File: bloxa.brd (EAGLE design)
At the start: 24.9 x 33.6 mm, 89 parts, among them CON1 PINHEAD_1X02-2.54, CON7 CON-4P-JST_GH-RA, CON8 CON-4P-JST_GH-RA, IC1 TPD3S014DBVR-SOT23-6, IC2 TJA1051(X)/3-SO8, IC6 MCP9700, Q13 BUK9K6R2-40E,115, Q14 BUK9K6R2-40E,115, Q15 BUK9K6R2-40E,115

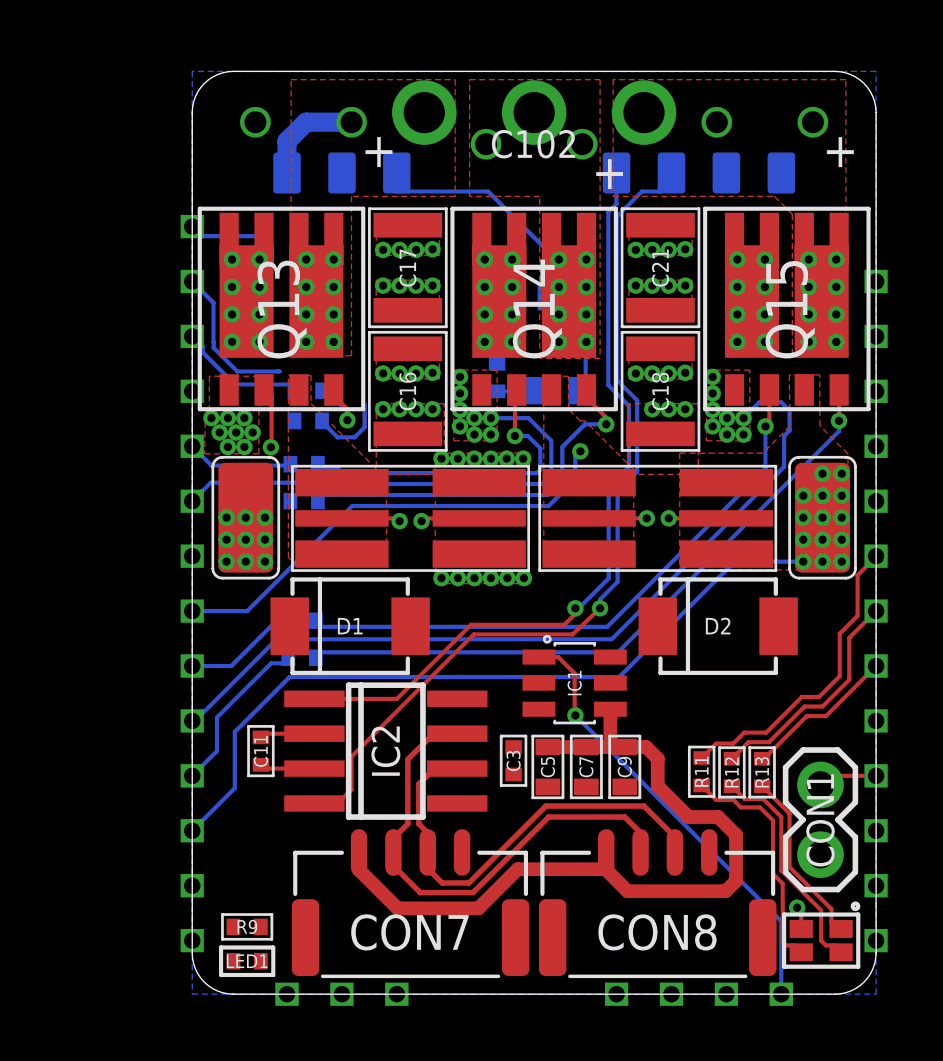
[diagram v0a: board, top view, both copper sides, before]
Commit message: all components moved to top side
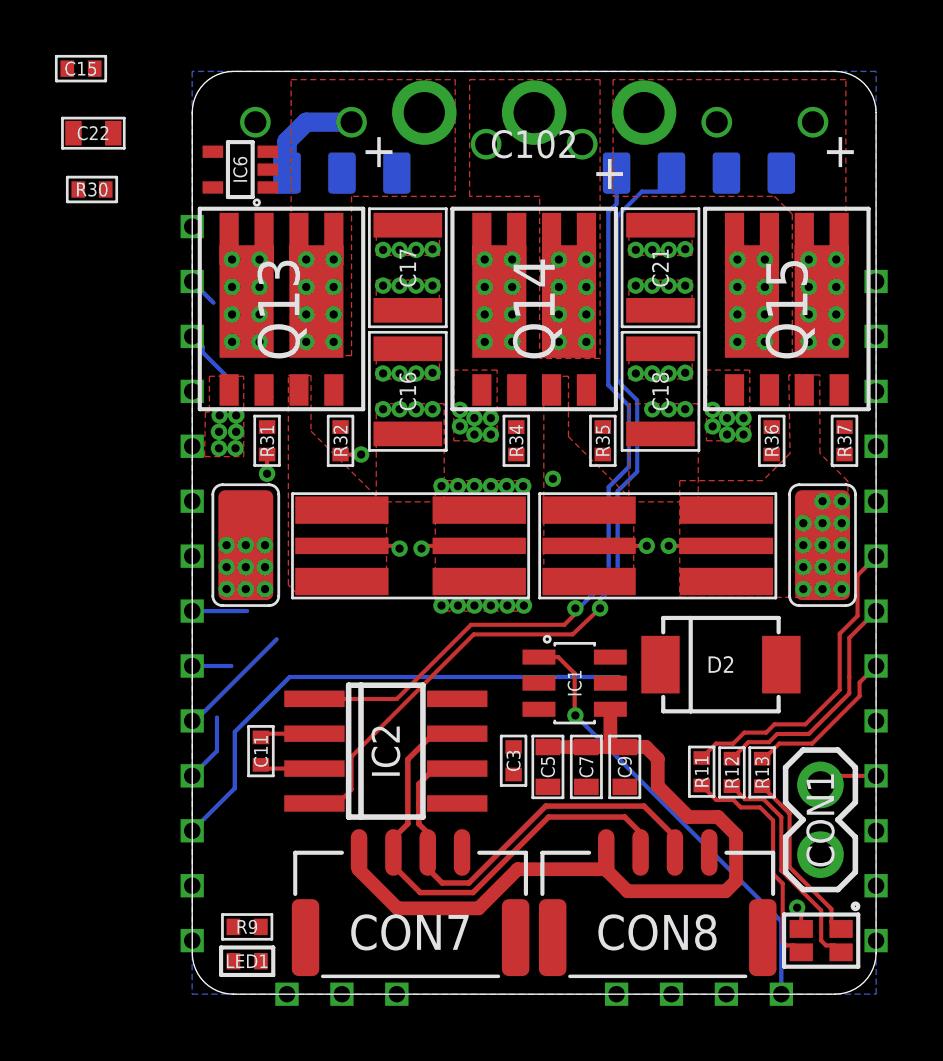
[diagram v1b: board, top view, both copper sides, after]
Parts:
- removed D1: PTVS36VP1UP,115-36V-SOD128, TVS_diodes:SOD128
- IC6: value MCP9700 -> MCP9700-SC70-5; device myxa_masterlib:SOT23B-3 -> misc:SC70-5
- moved R37 21.3 mm to (11.3, 5.20), flipped to the top, turned to 90 degrees
- moved C15 18.9 mm to (-16.5, 18.8), flipped to the top, turned to 180 degrees
- moved R36 18.3 mm to (8.65, 5.20), flipped to the top, turned to 90 degrees
- moved C22 18.2 mm to (-16.1, 16.4), flipped to the top
- moved R30 17.7 mm to (-16.1, 14.3), flipped to the top
- moved IC6 13.4 mm to (-10.7, 15.1), flipped to the top, turned to 180 degrees
- moved R35 11.1 mm to (2.50, 5.20), flipped to the top, turned to 90 degrees
- moved R34 7.77 mm to (-0.65, 5.20), flipped to the top, turned to 90 degrees
- moved R32 2.17 mm to (-7.05, 5.20), flipped to the top, turned to 90 degrees
- moved R31 1.67 mm to (-9.72, 5.20), flipped to the top, turned to 90 degrees
- moved D2 1.40 mm to (6.80, -2.95)
- moved BAT+ 1.00 mm to (-10.5, 1.40)
- moved BAT- 1.00 mm to (10.5, 1.40)
- moved R26 1.00 mm to (-4.50, 1.38)
- moved R33 1.00 mm to (4.50, 1.38)
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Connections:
- net N$1: now also IC6.4; no longer IC6.1
- net PGND: now also IC6.2; no longer D1.A, IC6.3
- net TEMPERATURE_SENSOR: now also IC6.3; no longer IC6.2
- net VDC: no longer D1.C
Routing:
- net PHASE_C: track 29.6 -> 4.31 mm, vias 16 -> 14
- net N$29: track 24.0 -> 0.00 mm, vias 1 -> 0
- net N$28: track 21.8 -> 0.00 mm, vias 1 -> 0
- net PHASE_B: track 18.4 -> 1.12 mm, vias 16 -> 14
- net PHASE_B_GND: track 17.0 -> 2.00 mm
- net N$31: track 14.1 -> 0.28 mm, vias 1 -> 0
- net N$30: track 11.9 -> 0.09 mm, vias 1 -> 0
- net PHASE_C_GND: track 27.5 -> 19.1 mm
- net VDD_5V: track 10.5 -> 2.84 mm
- net PHASE_A_GATE_HIGH: track 5.56 -> 0.70 mm, vias 0 -> 1
- net N$1: track 4.69 -> 0.00 mm
- net PHASE_A: track 5.96 -> 1.55 mm, vias 16 -> 14
- net PHASE_B_GATE_HIGH: track 3.89 -> 0.00 mm
- net PHASE_C_GATE_LOW: track 6.06 -> 2.50 mm
- net PHASE_C_GATE_HIGH: track 4.18 -> 1.42 mm
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
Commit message: routing complete
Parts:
- removed C22: 4.7µF, C_digikey:C0603
- removed R30: 200R, R_digikey:R0402
- added C1: 0.1µF, C_digikey:C0402
- moved C15 6.25 mm to (-10.3, 18.0), turned to 0 degrees
- moved R13 3.65 mm to (11.2, -4.70)
- moved S2 3.20 mm to (9.80, 3.00), flipped to the bottom
- moved R11 1.31 mm to (7.40, -6.97)
- moved R12 1.28 mm to (8.47, -6.97)
- moved C9 1.16 mm to (4.45, -6.55)
- moved C5 1.16 mm to (1.65, -6.55)
- moved C7 1.16 mm to (3.05, -6.55)
- moved C11 1.05 mm to (-9.95, -5.05)
- moved IC2 1.00 mm to (-5.40, -5.10)
- moved C3 0.72 mm to (-0.33, -5.88), turned to 180 degrees
- moved R34 0.30 mm to (-0.35, 5.20)
- moved R9 0.25 mm to (-10.4, -12.2), turned to 180 degrees
- moved D2 0.18 mm to (6.95, -2.85)
- turned LED1 to 0 degrees
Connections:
- removed net N$1: C22.P$2, IC6.4, R30.1
- removed net N$5: CON7.4, CON8.4
- net GND: no longer C11.2, C3.2, IC2.2
- net GNDD: now also CON7.4, CON8.4
- net PGND: now also C1.2, C11.2, C15.2, C3.2, IC2.2; no longer C15.1, C22.P$1
- net TEMPERATURE_SENSOR: now also C1.1; no longer C15.2
- net VDD_5V: now also C15.1, IC6.4; no longer R30.2
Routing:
- net VDD_5V: track 2.84 -> 76.3 mm, vias 1 -> 8
- net CAN1_LED: track 0.00 -> 45.8 mm, vias 0 -> 1
- net TEMPERATURE_SENSOR: track 0.00 -> 41.0 mm, vias 0 -> 2
- net PHASE_C_GATE_LOW: track 2.50 -> 29.7 mm, vias 0 -> 1
- net PHASE_C_GATE_HIGH: track 1.42 -> 25.0 mm, vias 0 -> 1
- net PHASE_C: track 4.31 -> 27.0 mm
- net PHASE_B_GATE_LOW: track 0.00 -> 20.5 mm, vias 0 -> 1
- net PHASE_B_GATE_HIGH: track 0.00 -> 14.7 mm, vias 0 -> 1
- net PHASE_B_GND: track 2.00 -> 16.4 mm
- net PGND: track 0.00 -> 13.0 mm, vias 40 -> 44
- net PHASE_B: track 1.12 -> 13.3 mm
- net PHASE_A_GATE_HIGH: track 0.70 -> 11.8 mm
- net PHASE_C_GND: track 19.1 -> 28.7 mm
- net PHASE_A_GATE_LOW: track 3.14 -> 12.8 mm
- net PHASE_A_GND: track 0.00 -> 9.05 mm, vias 0 -> 1
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- added copper zone on layer 1, net GNDD
- added copper zone on layer 16, net GNDD
- added copper zone on layer 15, net PHASE_A
- added copper zone on layer 15, net PHASE_B
- added copper zone on layer 15, net PHASE_C

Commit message: UPDATES
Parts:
- added U$1: CONNECTION, misc:CONNECTION
- added U$8, U$9: FIDUCIALMOUNT, usb2can_master_lib:FIDUCIA-MOUNT
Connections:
- net GNDD: now also U$1.P$2
- net PGND: now also U$1.P$1
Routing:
- net TEMPERATURE_SENSOR: track 41.0 -> 42.2 mm
- net VDD_5V: track 76.3 -> 75.4 mm
- net VDC: vias 52 -> 50
- net PGND: vias 44 -> 49
- net GNDD: vias 9 -> 12
- added copper zone on layer 1, net VDD_5V
- added copper zone on layer 15, net VDD_5V
- added copper zone on layer 16, net VDD_5V

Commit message: More polygones updates
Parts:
- added U$3: CONNECTION, misc:CONNECTION
- moved U$1 3.99 mm to (-6.78, -7.80), turned to 180 degrees
- turned CON1 to 270 degrees
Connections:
- net GND: now also C1.2, C11.2, C3.2, CON1.1, IC2.2, U$1.P$1, U$3.P$1
- net PGND: now also U$3.P$2; no longer C1.2, C11.2, C3.2, CON1.1, IC2.2, U$1.P$1
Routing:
- net PGND: track 13.0 -> 4.58 mm, vias 49 -> 38
- net GND: track 0.00 -> 6.58 mm, vias 0 -> 8
- net PHASE_B_CURRENT_SHUNT_P: track 24.1 -> 29.3 mm
- net PHASE_B_CURRENT_SHUNT_N: track 24.1 -> 29.0 mm
- net GNDD: track 0.05 -> 2.55 mm, vias 12 -> 10
- net PHASE_C_GATE_LOW: track 29.7 -> 32.0 mm
- net PHASE_C_GND: track 28.7 -> 30.7 mm
- net GPIO1: track 2.16 -> 3.71 mm
- net PHASE_C: track 27.0 -> 28.4 mm
- net VDD_5V: track 75.4 -> 76.4 mm
- net PHASE_A_GND: track 9.20 -> 9.96 mm
- net TEMPERATURE_SENSOR: track 42.2 -> 42.9 mm
- net CAN1_RX: track 30.6 -> 31.3 mm
- net VDC: vias 50 -> 49
- added copper zone on layer 15, net GND
- added copper zone on layer 16, net GND
- added copper zone on layer 15, net GNDD
- added copper zone on layer 16, net PHASE_A
- added copper zone on layer 16, net PHASE_B
- added copper zone on layer 16, net PHASE_C
- added copper zone on layer 15, net VDC
- added copper zone on layer 16, net VDC
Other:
- board text added: "BLOXA 0.1"

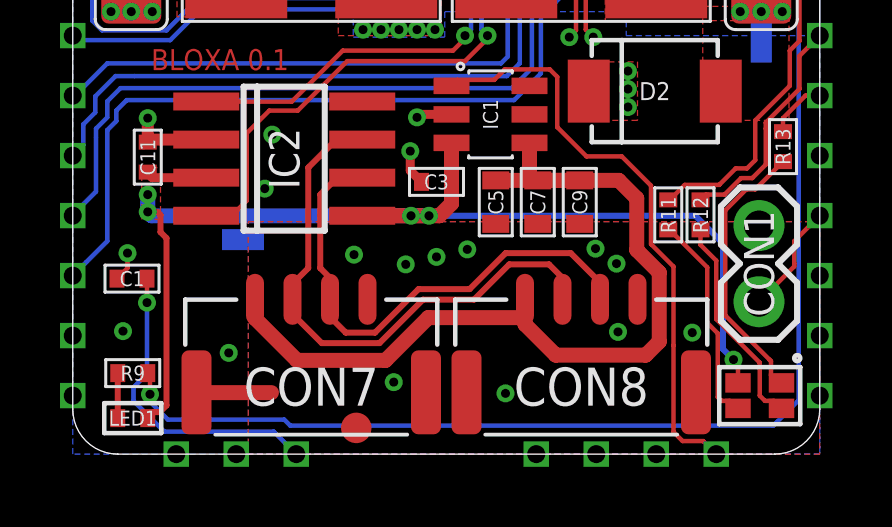
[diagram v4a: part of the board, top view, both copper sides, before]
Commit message: alternate footprints for LED fancy placement
Will never use it probably
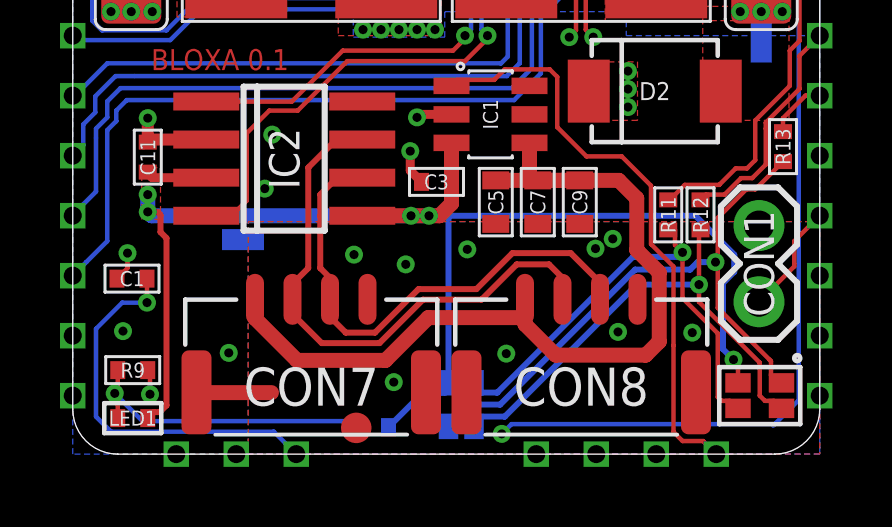
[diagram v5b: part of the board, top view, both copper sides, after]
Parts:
- added LED2: GREEN, myxa_masterlib:0402_LED
- added LED4: LTST-C19HE1WT, myxa_masterlib:LITE_ON_RGB_LED
- moved R9 0.10 mm to (-10.4, -12.2)
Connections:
- removed net N$59: LED3.G, R12.1
- new net N$4: LED3.G, LED4.G, R12.1
- net N$17: now also LED2.C
- net N$58: now also LED4.R
- net N$60: now also LED4.B
- net VDD_5V: now also LED2.A, LED4.+
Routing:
- net N$4: track 0.00 -> 16.9 mm, vias 0 -> 1
- net N$58: track 9.18 -> 20.8 mm, vias 0 -> 1
- net N$60: track 7.12 -> 16.5 mm, vias 0 -> 1
- net N$17: track 1.50 -> 10.3 mm, vias 0 -> 1
- net VDD_5V: track 76.4 -> 85.0 mm
- net N$59: track 7.24 -> 0.00 mm
- net TEMPERATURE_SENSOR: track 42.9 -> 45.5 mm
- net CAN1_LED: track 45.8 -> 46.1 mm, vias 1 -> 2
- net GNDD: vias 10 -> 9

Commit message: Renaming
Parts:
- removed C100, C101: 180µF, rc:RADIAL_SIDE_8X21.5
- removed C15: 0.1µF, C_digikey:C0402
- removed C16, C18: 10µF, C_digikey:C1210
- removed CON7: CON-4P-JST_GH-RA, Connectors:JST_GH-4P-RA
- removed IC6: MCP9700-SC70-5, misc:SC70-5
- removed R35, R36, R37: 4R3, R_digikey:R0402
- removed U$8, U$9: FIDUCIALMOUNT, usb2can_master_lib:FIDUCIA-MOUNT
- added C10, C4: 0.1µF, C_digikey:C0402
- added C12, C13, C14: 4.7µF, C_digikey:C0603
- added CON3: PINHEAD_1X02-2.54, pinhead:1X02-PTH-2.54
- added FD1, FD2: FIDUCIALMOUNT, misc:FIDUCIA-MOUNT
- added IC3: TJA1051(X)/3-SO8, serial_interfaces:SOIC8
- added R3, R5, R6: 1K, R_digikey:R0402
- C1, C3: value 0.1µF -> 180µF; device C_digikey:C0402 -> rc:RADIAL_SIDE_8X21.5
- C5: value 4.7µF -> 0.1µF; device C_digikey:C0603 -> C_digikey:C0402
- C7, C9: value 4.7µF -> 10µF; device C_digikey:C0603 -> C_digikey:C1210
- CON1: value PINHEAD_1X02-2.54 -> CON-4P-JST_GH-RA; device pinhead:1X02-PTH-2.54 -> Connectors:JST_GH-4P-RA
- IC1: value TPD3S014DBVR-SOT23-6 -> MCP9700-SC70-5; device myxa_masterlib:SOT26 -> misc:SC70-5
- IC2: value TJA1051(X)/3-SO8 -> TPD3S014DBVR-SOT23-6; device serial_interfaces:SOIC8 -> myxa_masterlib:SOT26
- PAD22, PAD23, PAD24, PAD4: value PAD-HOLE-0.6 -> PAD-1X1.5; device PADS:HOLE_0.6 -> PADS:SMD_1X1,5
- PAD38, PAD39, PAD40, PAD41: value PAD-1X1.5 -> PAD-HOLE-0.6; device PADS:SMD_1X1,5 -> PADS:HOLE_0.6
- R11, R12, R9: value 1K -> 4R3
- moved PAD25 36.0 mm to (-12.4, 13.0)
- moved PAD38 35.2 mm to (-12.4, -13.0)
- moved PAD24 34.9 mm to (-9.00, 14.9)
- moved PAD39 33.9 mm to (-9.00, -14.9)
- moved PAD26 33.2 mm to (-12.4, 11.0)
- moved PAD37 33.2 mm to (-12.4, -11.0)
- moved PAD23 33.0 mm to (-7.00, 14.9)
- moved PAD40 32.2 mm to (-7.00, -14.9)
- moved PAD22 31.5 mm to (-5.00, 14.9)
- moved PAD41 31.0 mm to (-5.00, -14.9)
- moved PAD27 30.7 mm to (-12.4, 9.00)
- moved PAD36 30.7 mm to (-12.4, -9.00)
- moved PAD28 28.6 mm to (-12.4, 7.00)
- moved PAD35 28.6 mm to (-12.4, -7.00)
- moved C5 27.3 mm to (-10.3, 18.0), turned to 0 degrees
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- renumbered A to PAD44, B to PAD45, BAT+ to PAD42, BAT- to PAD43, C to PAD46, C102 to C2, C17 to C8, C21 to C6, CON8 to CON2, D2 to D1, Q13 to Q1, Q14 to Q2, Q15 to Q3, R13 to R7, R26 to R4, R31 to R1, R32 to R2, R33 to R10, R34 to R8, S2 to S1, U$1 to J2, U$3 to J1
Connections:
- net BEC_ENABLE_OUT: now also IC2.1, PAD21.P$1; no longer IC1.1, PAD24.P$1
- net CAN1_LED: now also PAD6.P$1, R3.1; no longer PAD36.P$1, R9.1
- net CAN1_RX: now also IC3.4, PAD2.P$1; no longer IC2.4, PAD40.P$1
- net CAN1_TX: now also IC3.1, PAD1.P$1; no longer IC2.1, PAD41.P$1
- net CAN1_VDD: now also C12.P$2, C13.P$2, C14.P$2, CON1.1, IC2.4; no longer C5.P$2, C7.P$2, C9.P$2, CON7.1, IC1.4
- net CAN2_LED: now also PAD5.P$1; no longer PAD37.P$1
- net CAN2_RX: now also PAD4.P$1; no longer PAD38.P$1
- net CAN2_TX: now also PAD3.P$1; no longer PAD39.P$1
- net EN_GATE_OUT: now also PAD16.P$1; no longer PAD26.P$1
- net GAIN_OUT: now also PAD17.P$1; no longer PAD25.P$1
- net GND: now also C10.2, C4.2, CON3.1, IC3.2; no longer C1.2, C3.2, CON1.1, IC1.2
- net GNDD: now also C12.P$1, C13.P$1, C14.P$1, CON1.4, CON1.M$0, CON1.M$1; no longer C5.P$1, C7.P$1, C9.P$1, CON7.4, CON7.M$0, CON7.M$1
- net GPIO1: now also CON3.2, PAD14.P$1; no longer CON1.2, PAD28.P$1
- net GPIO2: now also PAD15.P$1; no longer PAD27.P$1
- net N$17: now also R3.2; no longer R9.2
- net N$2: now also IC3.8; no longer IC2.8
- net N$22: now also CON1.2, IC3.7; no longer CON7.2, IC2.7
- net N$23: now also CON1.3, IC3.6; no longer CON7.3, IC2.6
- net N$28: now also R11.2; no longer R36.2
- net N$29: now also R12.2; no longer R37.2
- net N$31: now also R9.2; no longer R35.2
- net N$4: now also R6.1; no longer R12.1
- net N$60: now also R5.1; no longer R11.1
- net OVERCURRENT_PROTECT_ADJ: now also PAD13.P$1; no longer PAD29.P$1
- net PGND: now also C1.-, C3.-, C5.2, C7.1, C9.1, IC1.2, PAD23.P$1; no longer C100.-, C101.-, C15.2, C16.1, C18.1, IC6.2, PAD2.P$1
- net PHASE_A: now also PAD26.P$1; no longer PAD5.P$1
- net PHASE_A_CURRENT_SHUNT_N: now also PAD37.P$1; no longer PAD16.P$1
- net PHASE_A_CURRENT_SHUNT_P: now also PAD38.P$1; no longer PAD17.P$1
- net PHASE_A_GATE_HIGH: now also PAD25.P$1; no longer PAD4.P$1
- net PHASE_A_GATE_LOW: now also PAD27.P$1; no longer PAD6.P$1
- net PHASE_A_GND: now also PAD28.P$1; no longer PAD7.P$1
- net PHASE_B: now also PAD30.P$1; no longer PAD9.P$1
- net PHASE_B_CURRENT_SHUNT_N: now also PAD39.P$1; no longer PAD18.P$1
- net PHASE_B_CURRENT_SHUNT_P: now also PAD40.P$1; no longer PAD19.P$1
- net PHASE_B_GATE_HIGH: now also PAD29.P$1; no longer PAD8.P$1
- net PHASE_B_GATE_LOW: now also PAD31.P$1, R9.1; no longer PAD10.P$1, R35.1
- net PHASE_B_GND: now also PAD32.P$1; no longer PAD11.P$1
- net PHASE_C: now also PAD34.P$1; no longer PAD13.P$1
- net PHASE_C_GATE_HIGH: now also PAD33.P$1, R11.1; no longer PAD12.P$1, R36.1
- net PHASE_C_GATE_LOW: now also PAD35.P$1, R12.1; no longer PAD14.P$1, R37.1
- net PHASE_C_GND: now also PAD36.P$1; no longer PAD15.P$1
- net POWER_ENABLE_IN: now also PAD18.P$1; no longer PAD21.P$1
- net RGB_LED_B: now also PAD10.P$1, R5.2; no longer PAD32.P$1, R11.2
- net RGB_LED_G: now also PAD11.P$1, R6.2; no longer PAD31.P$1, R12.2
- net RGB_LED_R: now also PAD12.P$1; no longer PAD30.P$1
- net TEMPERATURE_SENSOR: now also C4.1, IC1.3, PAD41.P$1; no longer C1.1, IC6.3, PAD20.P$1
- net USART_RX: now also PAD20.P$1; no longer PAD23.P$1
- net USART_TX: now also PAD19.P$1; no longer PAD22.P$1
- net USB+: now also PAD7.P$1; no longer PAD35.P$1
- net USB-: now also PAD8.P$1; no longer PAD34.P$1
- net USB_VBUS: now also PAD9.P$1; no longer PAD33.P$1
- net VDC: now also C1.+, C3.+, C7.2, C9.2, PAD24.P$1; no longer C100.+, C101.+, C16.2, C18.2, PAD3.P$1
- net VDD_5V: now also C10.1, C5.1, IC1.4, IC3.3, IC3.5, PAD22.P$1; no longer C15.1, C3.1, IC1.3, IC2.5, IC6.4, PAD1.P$1
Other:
- board text added: "+"
- board text added: "C1"
- board text added: "C2"
- board text added: "C3"
